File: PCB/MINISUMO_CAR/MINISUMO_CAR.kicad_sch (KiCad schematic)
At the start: 4 parts

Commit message: ADD pad of battery
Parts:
- BT1: now left out of the parts list
- TP1, TP3: footprint (none) -> TestPoint:TestPoint_THTPad_3.0x3.0mm_Drill1.5mm

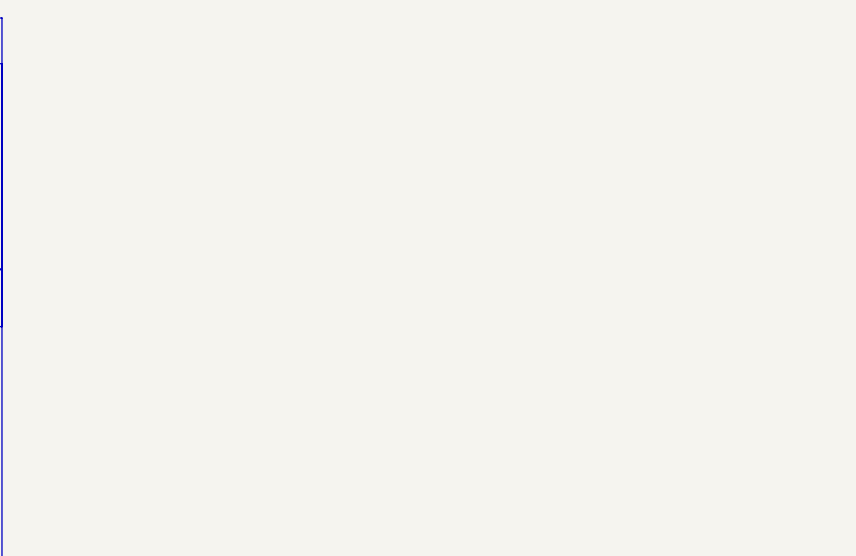
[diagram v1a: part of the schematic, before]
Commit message: add sensors  HC-SR04
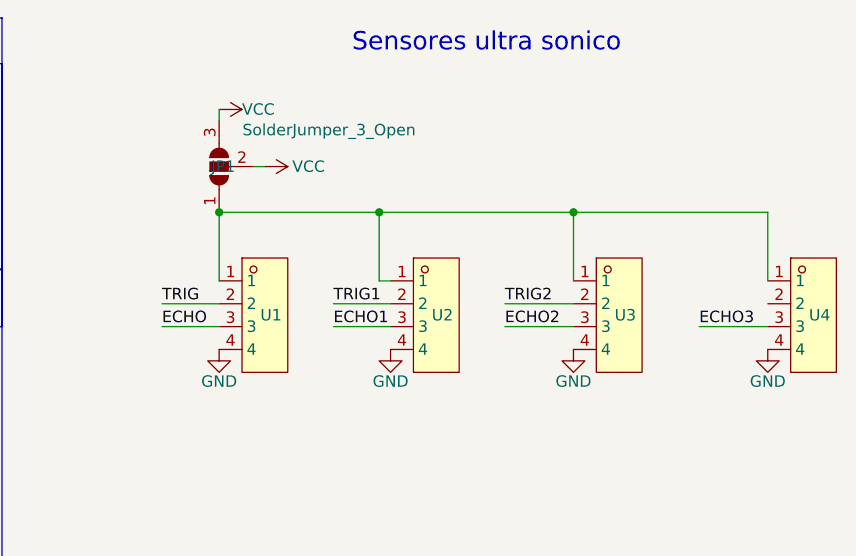
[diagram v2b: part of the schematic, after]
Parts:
- added JP1: SolderJumper_3_Open, symbol Jumper:SolderJumper_3_Open
- added U1, U2, U3, U4: XY-XHB2.54-4A11, EasyEDA:HDR-TH_4P-P2.50-V-F-2, symbol EasyEDA:XY-XHB2.54-4A11
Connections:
- net -BATT: now also U1.4, U2.4, U3.4, U4.4
- new net: JP1.1 (A), U1.1, U2.1, U3.1, U4.1
- new net ECHO: U1.3
- new net ECHO1: U2.3
- new net ECHO2: U3.3
- new net ECHO3: U4.3
- new net TRIG: U1.2
- new net TRIG1: U2.2
- new net TRIG2: U3.2
- new net VCC: JP1.2 (C), JP1.3 (B)
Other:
- note added: "Sensores ultra sonico"

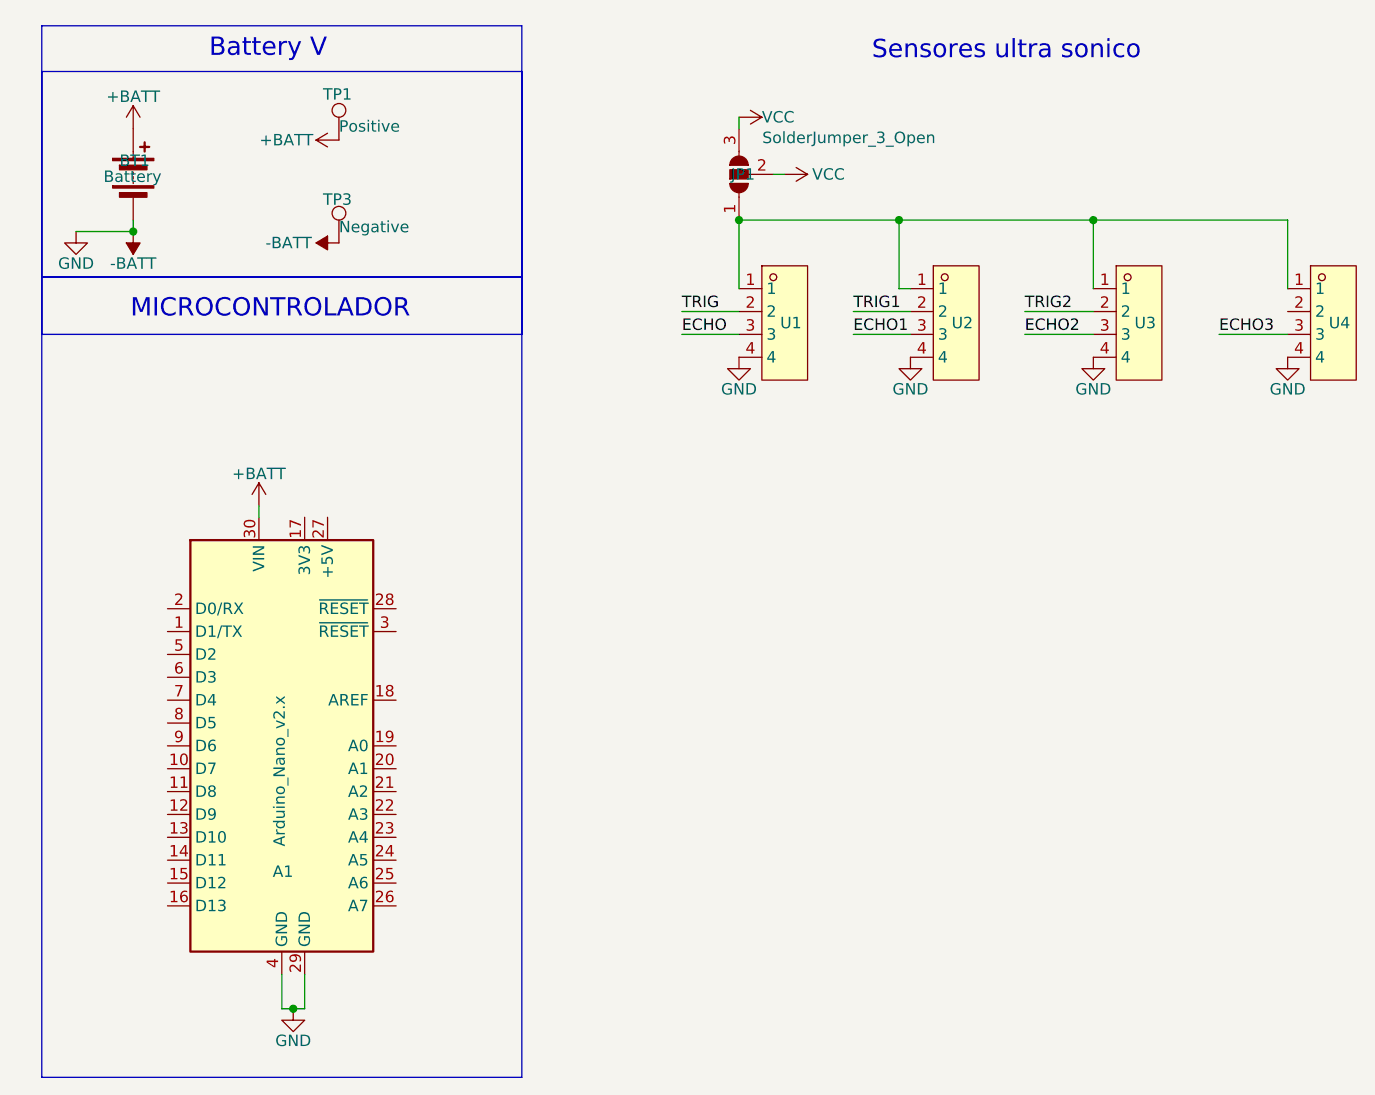
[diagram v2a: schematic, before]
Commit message: add sensor infrarojo
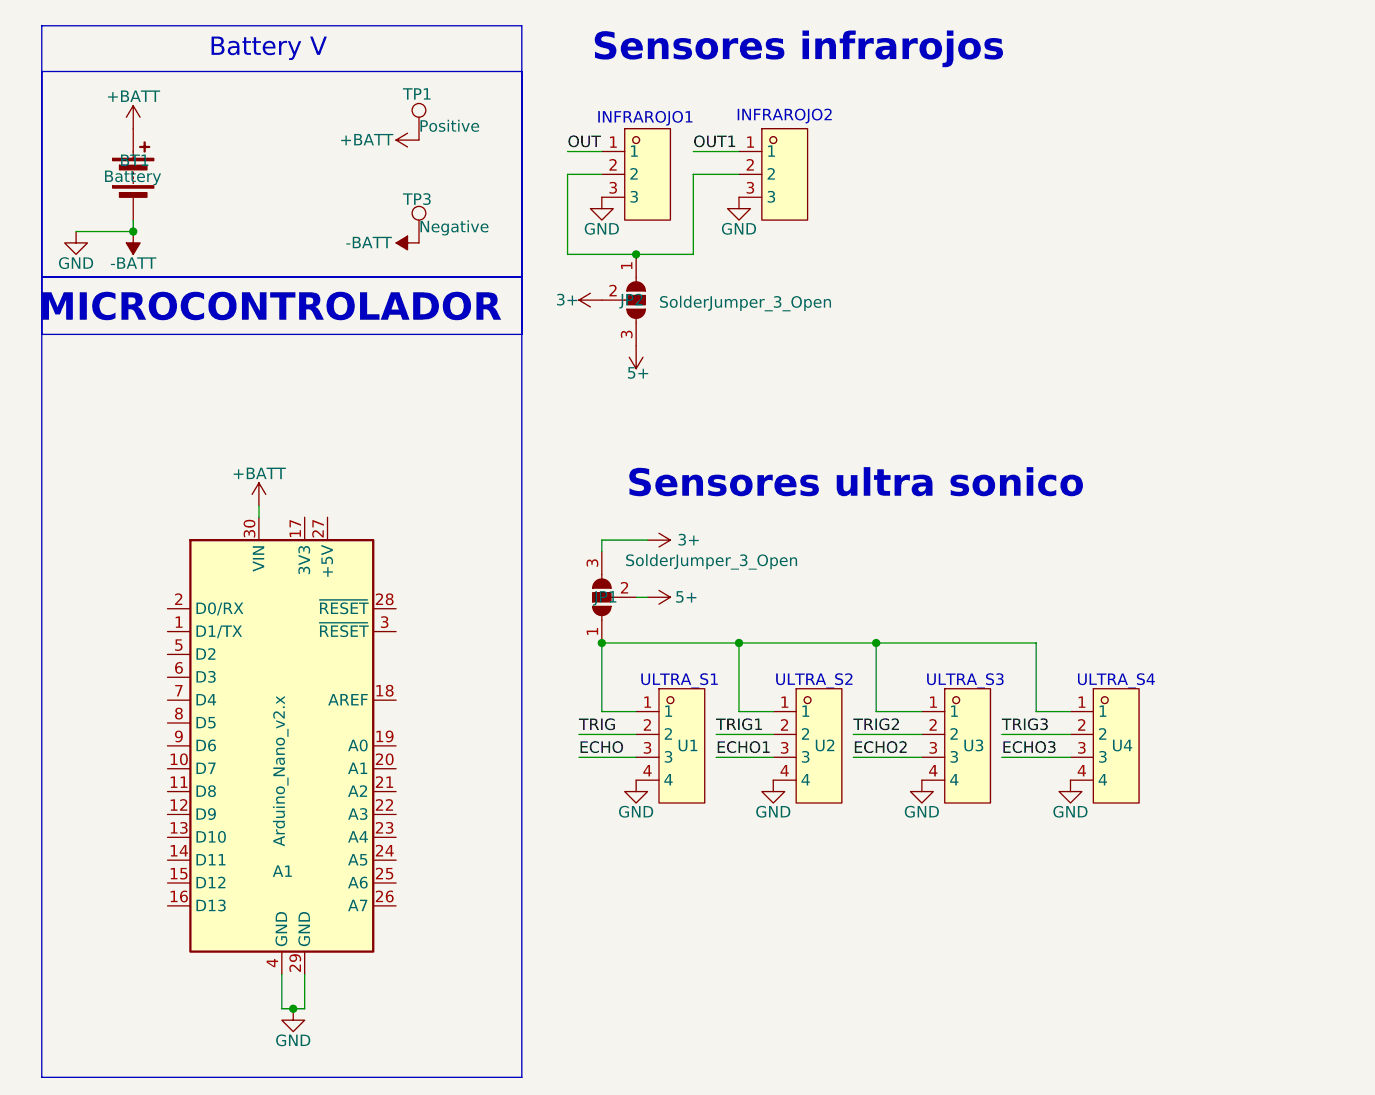
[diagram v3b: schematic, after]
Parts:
- added JP2: SolderJumper_3_Open, symbol Jumper:SolderJumper_3_Open
- added U5, U6: XY-XHB2.54-3A11, EasyEDA:CONN-TH_3P-P2.50_XY-XHB2.54-3A11, symbol EasyEDA:XY-XHB2.54-3A11
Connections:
- net -BATT: now also U5.3, U6.3
- net TRIG3: now reaches U4.2
- net VCC renamed 3+
- net 3+: now also JP2.2 (C); no longer JP1.2 (C)
- new net: JP2.1 (A), U5.2, U6.2
- new net 5+: JP1.2 (C), JP2.3 (B)
- new net OUT: U5.1
- new net OUT1: U6.1
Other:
- note added: "INFRAROJO1"
- note added: "INFRAROJO2"
- note added: "Sensores infrarojos"
- note added: "ULTRA_S1"
- note added: "ULTRA_S2"
- note added: "ULTRA_S3"
- note added: "ULTRA_S4"
- moved on the sheet: JP1, TP1, TP3, U1, U2, U3, U4
